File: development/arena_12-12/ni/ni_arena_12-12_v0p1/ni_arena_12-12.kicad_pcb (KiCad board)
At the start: 4 copper layers, 228.6 x 228.6 mm, 581 parts, among them J1 Barrel_Jack, J2 NI_TE_68pos, J3 Barrel_Jack, P1 CONN15, P10 CONN15, P11 CONN15, P12 CONN15, P2 CONN15, P3 CONN15, P4 CONN15, P5 CONN15, P6 CONN15, P7 CONN15, P8 CONN15, P9 CONN15, Q1 MOSFET_NCHAN, SW1 SW_SPDT, U1 AP2112K-3.3, U10 TXB0108PW, U100 74LVC2G17, U101 74LVC2G17, U102 74LVC2G17, U103 74LVC2G17, U104 74LVC2G17, U105 74LVC2G17, U106 74LVC2G17, U107 74LVC2G17, U108 74LVC2G17, U109 74LVC2G17, U11 TXB0108PW, U110 74LVC2G17, U12 TXB0108PW, U13 TXB0108PW, U14 TXB0108PW, U15 TXB0108PW, U16 TXB0108PW, U17 TXB0108PW, U18 TXB0108PW, U19 74LVC2G17, U2 TXB0108PW, U20 74LVC2G17, U21 74LVC2G17, U22 74LVC2G17, U23 74LVC2G17, U24 74LVC2G17, U25 74LVC2G17, U26 74LVC2G17, U27 74LVC2G17, U28 74LVC2G17, U29 74LVC2G17, U3 TXB0108PW, U30 74LVC2G17, U31 74LVC2G17, U32 74LVC2G17, U33 74LVC2G17, U34 74LVC2G17, U35 74LVC2G17, U36 74LVC2G17, U37 74LVC2G17, U38 74LVC2G17, U39 74LVC2G17, U4 TXB0108PW, U40 74LVC2G17, U41 74LVC2G17, U42 74LVC2G17, U43 74LVC2G17, U44 74LVC2G17, U45 74LVC2G17, U46 74LVC2G17, U47 74LVC2G17, U48 74LVC2G17, U49 74LVC2G17, U5 TXB0108PW, U50 74LVC2G17, U51 74LVC2G17, U52 74LVC2G17, U53 74LVC2G17, U54 74LVC2G17, U55 74LVC2G17, U56 74LVC2G17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

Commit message: Worked on layout of 12-12 NI arena with schmitt buffers.
Finished preliminary layout.
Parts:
- moved R104 374.6 mm to (72.5, 244.7), turned to -90 degrees
- moved R105 372.7 mm to (73.6, 244.7), turned to -90 degrees
- moved R106 370.8 mm to (74.7, 244.7), turned to -90 degrees
- moved R107 368.9 mm to (75.7, 244.7), turned to -90 degrees
- moved R108 367.0 mm to (76.8, 244.7), turned to -90 degrees
- moved R109 364.9 mm to (78.1, 244.8), turned to -90 degrees
- moved R101 364.7 mm to (68.2, 244.7), turned to -90 degrees
- moved R110 362.1 mm to (80.3, 244.8), turned to -90 degrees
- moved R102 361.9 mm to (70.4, 244.7), turned to -90 degrees
- moved R119 360.7 mm to (91.5, 244.7), turned to -90 degrees
- moved R111 360.2 mm to (81.3, 244.8), turned to -90 degrees
- moved R103 360.0 mm to (71.5, 244.7), turned to -90 degrees
- moved R120 358.7 mm to (92.6, 244.7), turned to -90 degrees
- moved R112 358.3 mm to (82.4, 244.8), turned to -90 degrees
- moved R121 356.8 mm to (93.7, 244.7), turned to -90 degrees
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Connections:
- U28 pad 1: /Level Shifters/PAN5V.MISO_00 -> /Level Shifters/PAN5V.MISO_01
- U28 pad 3: /Level Shifters/PAN5V.MISO_01 -> /Level Shifters/PAN5V.MISO_00
- U28 pad 4: Net-(U17-B2) -> Net-(U17-B1)
- U28 pad 6: Net-(U17-B1) -> Net-(U17-B2)
- U29 pad 1: /Level Shifters/PAN5V.MISO_02 -> /Level Shifters/PAN5V.MISO_03
- U29 pad 3: /Level Shifters/PAN5V.MISO_03 -> /Level Shifters/PAN5V.MISO_02
- U29 pad 4: Net-(U17-B4) -> Net-(U17-B3)
- U29 pad 6: Net-(U17-B3) -> Net-(U17-B4)
- U30 pad 1: /Level Shifters/PAN5V.MISO_04 -> /Level Shifters/PAN5V.MISO_05
- U30 pad 3: /Level Shifters/PAN5V.MISO_05 -> /Level Shifters/PAN5V.MISO_04
- U30 pad 4: Net-(U17-B6) -> Net-(U17-B5)
- U30 pad 6: Net-(U17-B5) -> Net-(U17-B6)

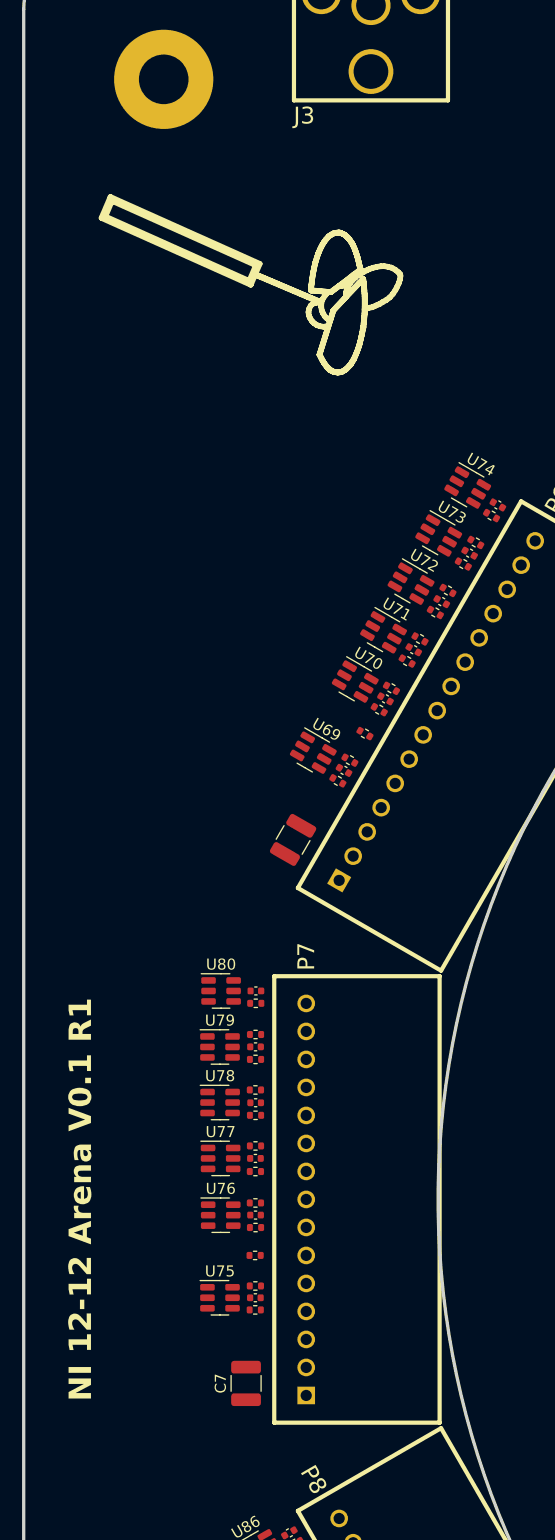
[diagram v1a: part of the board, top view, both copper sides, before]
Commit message: Worked on 12-12 NI arena with schmitt buffers.
Added silkscreen annotations.
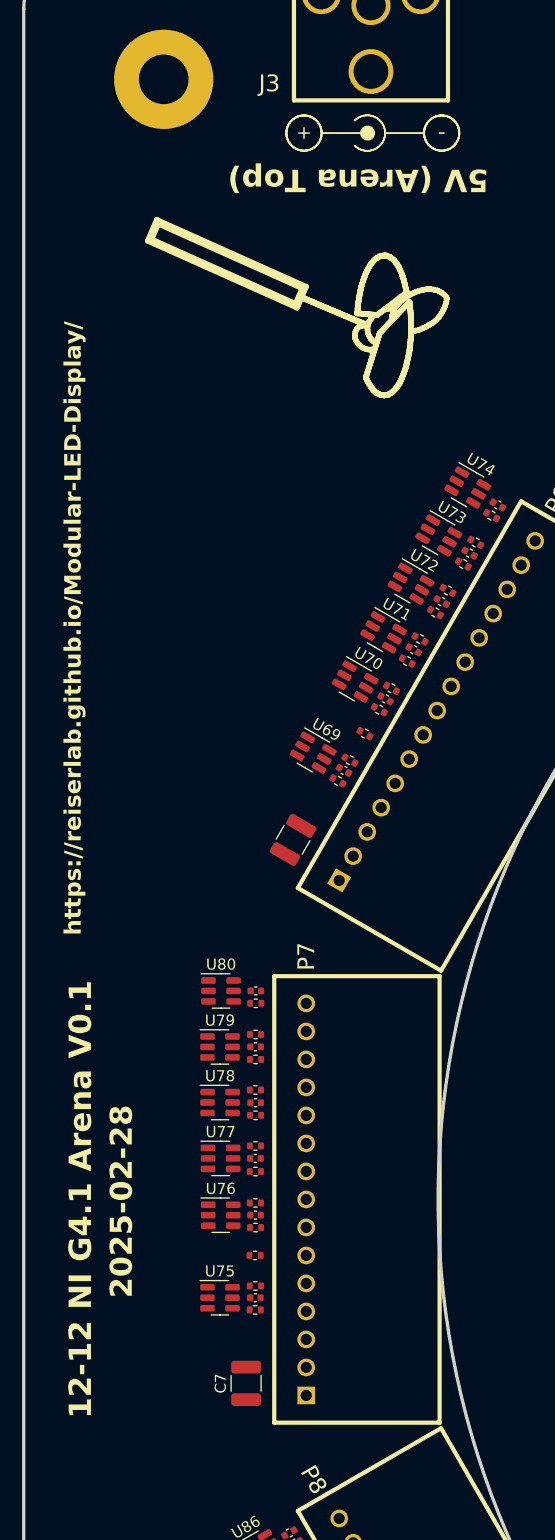
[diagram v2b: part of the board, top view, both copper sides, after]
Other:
- board text added: "12-12 NI G4.1 Arena V0.1"
- board text added: "2025-02-28"
- board text added: "5V (Arena Top)"
- board text added: "https://reiserlab.github.io/Modular-LED-Display/"
- board text removed: "NI 12-12 Arena V0.1 R1"

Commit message: Worked on routing and board setup.
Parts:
- moved R81 3.13 mm to (226.0, 275.4)
- moved R88 3.13 mm to (234.9, 275.4)
- moved R89 3.13 mm to (236.0, 275.4)
- moved R94 3.13 mm to (242.6, 275.3)
- moved C119 3.13 mm to (222.6, 287.0)
- moved C120 3.13 mm to (221.6, 275.4)
- moved C121 3.13 mm to (232.4, 287.3)
- moved C122 3.13 mm to (231.6, 275.4)
- moved C123 3.13 mm to (242.5, 287.2)
- moved R100 3.13 mm to (249.0, 275.3)
- moved R77 3.13 mm to (220.6, 275.3)
- moved R78 3.13 mm to (222.7, 275.4)
- moved R79 3.13 mm to (223.8, 275.4)
- moved R80 3.13 mm to (224.9, 275.4)
- moved R82 3.13 mm to (227.0, 275.4)
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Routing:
- net /Power & Voltage Regulators/SW_5V: track 0.00 -> 31.2 mm
- net +5V: track 0.00 -> 7.41 mm, vias 0 -> 1
- net +3.3V: track 0.00 -> 5.19 mm, vias 0 -> 1
- net GND: track 0.00 -> 4.34 mm, vias 0 -> 2
- added copper zone on In3.Cu, net +3.3V
- added copper zone on In4.Cu, net GND
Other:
- copper layers 4 -> 6

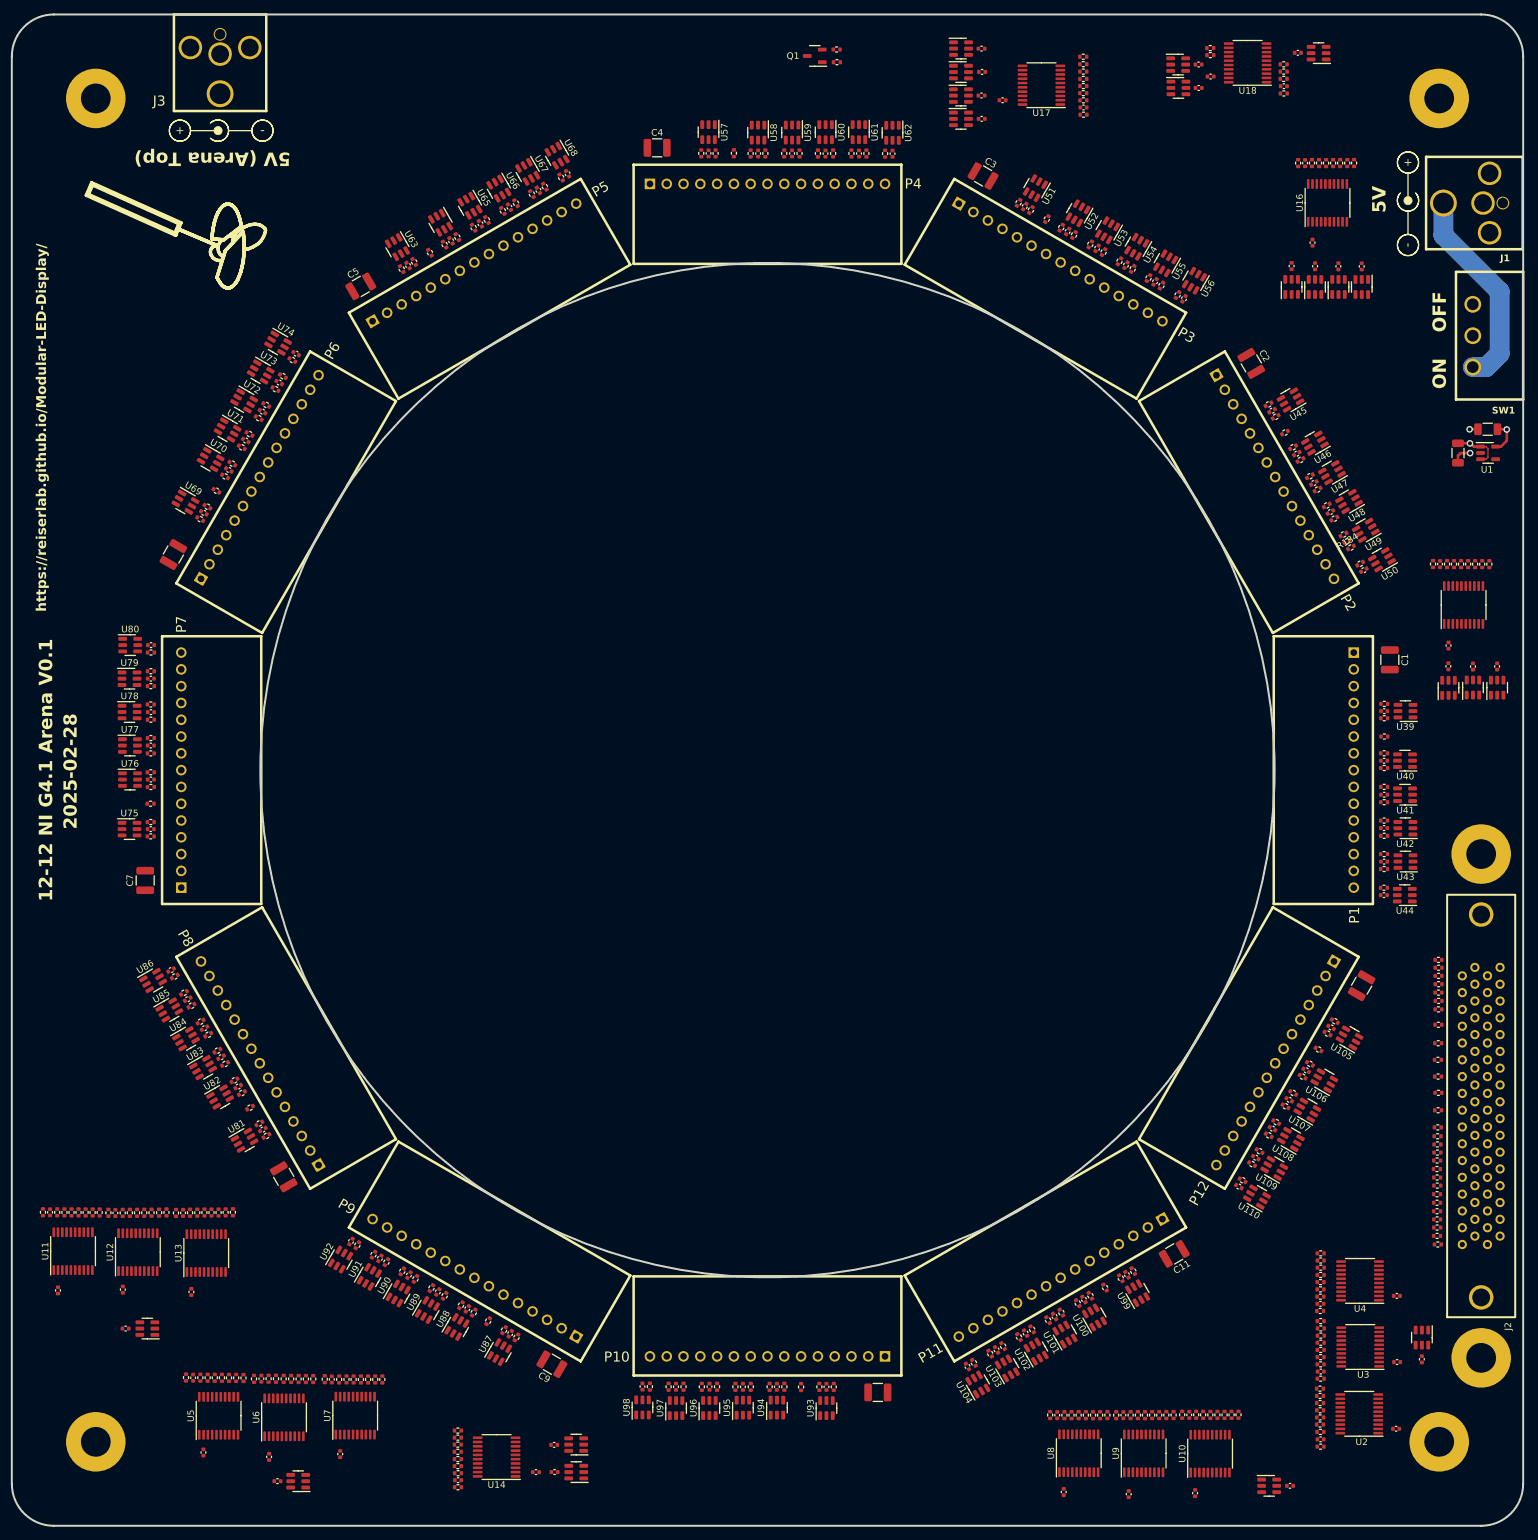
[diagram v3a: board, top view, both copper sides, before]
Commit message: Worked on routing for 12-12 NI arena.
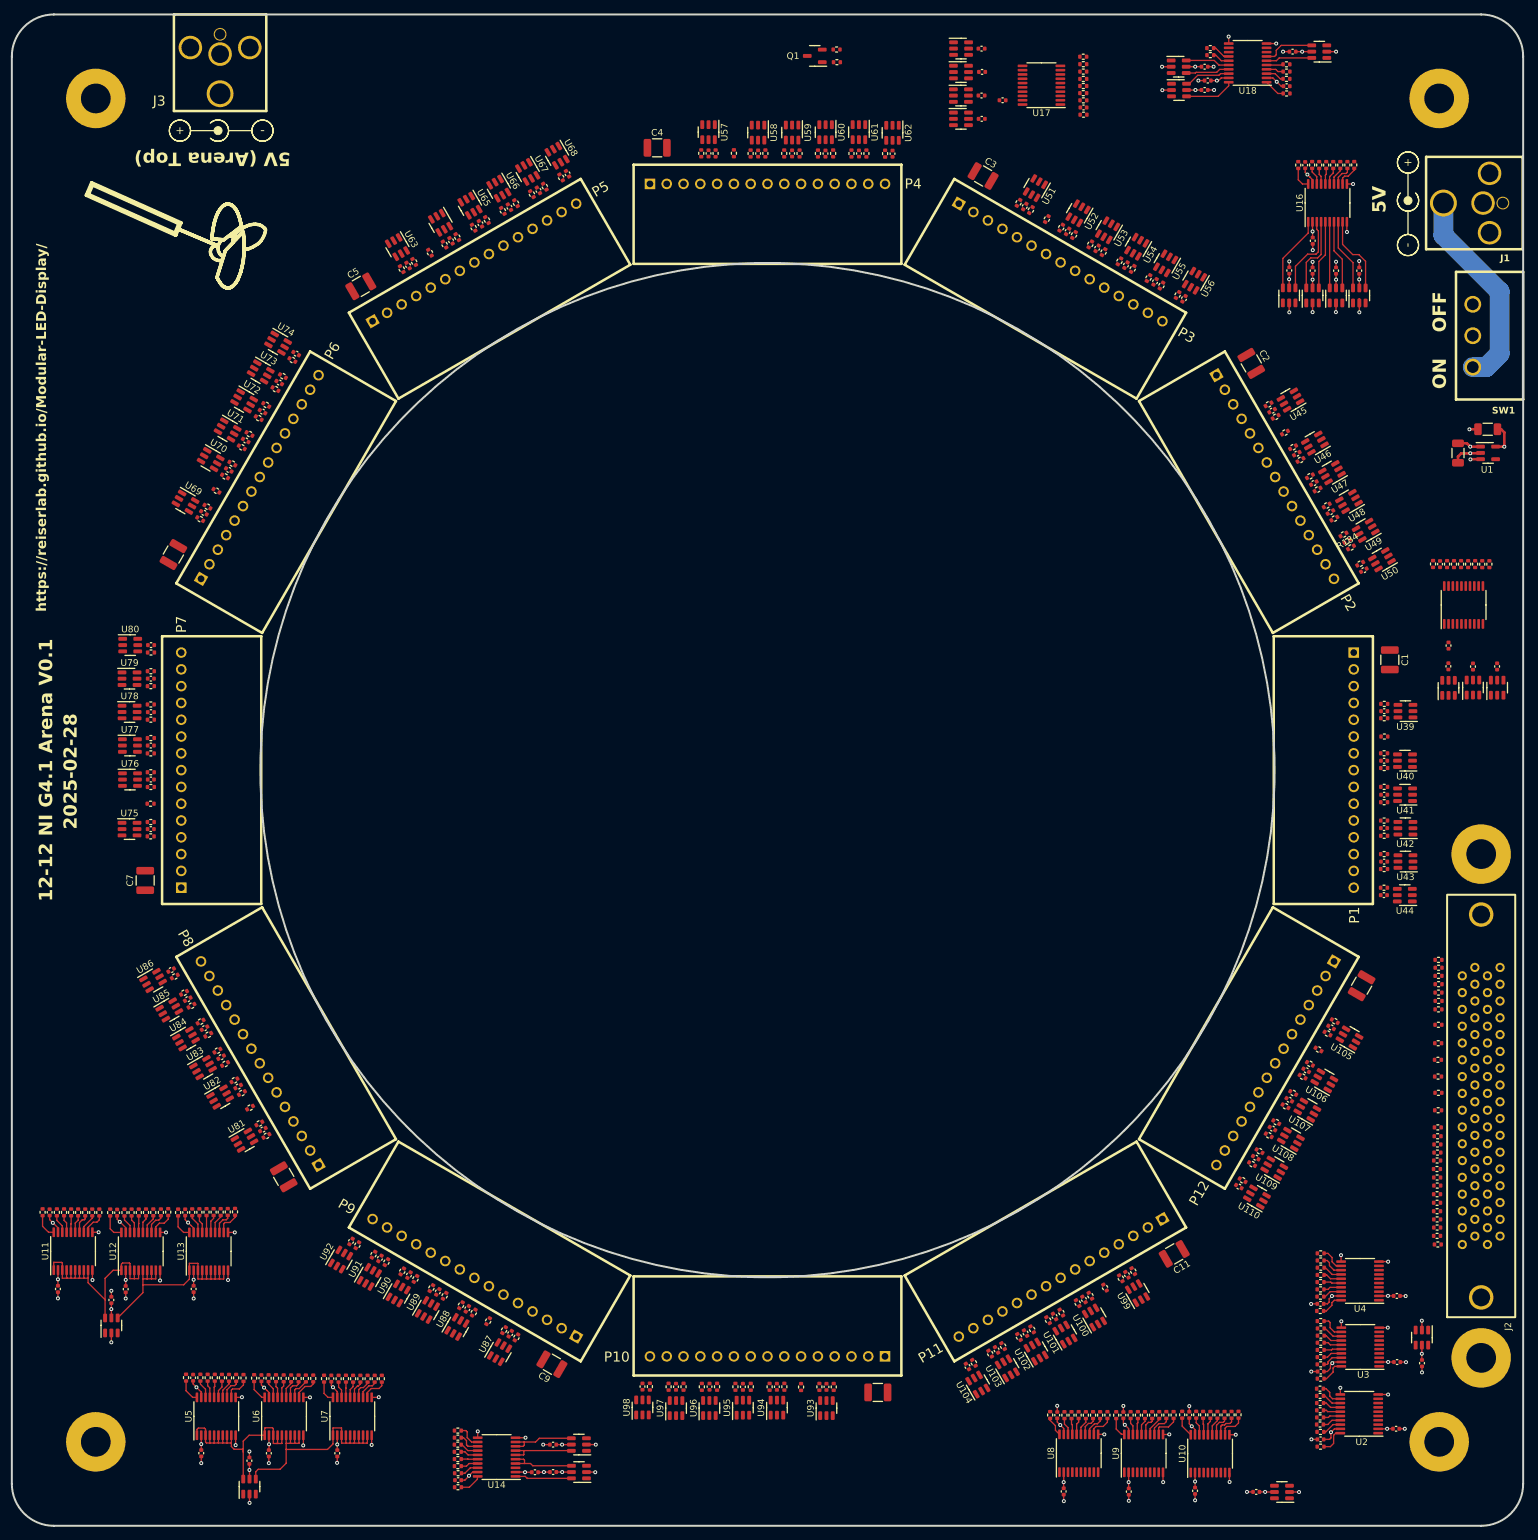
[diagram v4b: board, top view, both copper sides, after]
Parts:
- moved U20 7.41 mm to (99.5, 286.2), turned to 90 degrees
- moved U22 5.46 mm to (78.6, 261.8), turned to 90 degrees
- moved C16 5.25 mm to (99.4, 282.3), turned to 90 degrees
- moved C17 5.20 mm to (251.7, 287.0), turned to 180 degrees
- moved C18 4.83 mm to (78.5, 257.9), turned to 90 degrees
- moved U21 2.15 mm to (255.6, 287.0), turned to 180 degrees
- moved U32 1.33 mm to (256.7, 106.0)
- moved U33 1.33 mm to (263.8, 106.0)
- moved U34 1.33 mm to (260.2, 106.0)
- moved U35 1.33 mm to (267.3, 106.0), turned to 90 degrees
- moved C33 0.97 mm to (243.9, 71.4)
- moved C32 0.96 mm to (243.9, 74.9)
- moved C34 0.82 mm to (257.2, 69.1)
- moved C25 0.77 mm to (260.2, 102.2), turned to 90 degrees
- moved C24 0.76 mm to (256.7, 102.2), turned to 90 degrees
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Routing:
- net +3.3V: track 5.19 -> 85.8 mm, vias 1 -> 41
- net GND: track 4.34 -> 71.6 mm, vias 2 -> 63
- net +5V: track 7.41 -> 55.4 mm, vias 1 -> 19
- net Net-(U6-A5): track 0.00 -> 40.6 mm
- net Net-(U12-A5): track 0.00 -> 40.0 mm
- net Net-(U11-A1): track 0.00 -> 37.8 mm
- net Net-(U5-A1): track 0.00 -> 36.2 mm
- net Net-(U16-A2): track 0.00 -> 12.3 mm
- net Net-(U16-A8): track 0.00 -> 12.0 mm
- net Net-(U16-A1): track 0.00 -> 11.6 mm
- net Net-(U16-A3): track 0.00 -> 11.5 mm
- net Net-(U16-A7): track 0.00 -> 10.9 mm
- net Net-(U14-A7): track 0.00 -> 10.6 mm
- net Net-(U14-A3): track 0.00 -> 10.5 mm
- net Net-(U16-A6): track 0.00 -> 10.5 mm
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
